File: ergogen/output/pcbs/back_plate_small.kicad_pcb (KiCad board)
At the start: 2 copper layers, 127.5 x 91.9 mm, 6 parts

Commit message: new shape
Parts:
- removed ?: , solar_system
- moved MH4 15.9 mm to (104.5, 92.8), turned to 10 degrees
- moved MH3 15.6 mm to (143.4, 98.1), turned to -15 degrees
- moved MH2 6.89 mm to (127.1, 46.3)
- moved MH5 5.62 mm to (73.6, 78.6)
- moved MH1 2.52 mm to (90.5, 47.3)
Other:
- board size 127.5 x 91.9 mm -> 130.9 x 107.2 mm

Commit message: update generated files
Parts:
- moved MH3 20.0 mm to (160.6, 108.1), turned to -30 degrees
- moved MH4 19.6 mm to (124.1, 92.9), turned to 0 degrees
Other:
- outline, holes or cut-outs redrawn
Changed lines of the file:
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@@
   (title_block
     (title "back_plate_small")
-    (date "2025-11-10")
+    (date "2025-11-12")
     (rev "1")
     (company "curtis bollinger")
@@
   (footprint "ceoloide:mounting_hole_npth"
     (layer "F.Cu")
-    (at 143.3735818 98.05513279999998 -15)
+    (at 160.64669740000002 108.05669409999999 -30)
     (property "Reference" "MH3"
-      (at 0 2.55 -15)
+      (at 0 2.55 -30)
       (layer "F.SilkS")
       hide
@@
     )
     (pad "" np_thru_hole circle
-      (at 0 0 -15)
+      (at 0 0 -30)
       (size 2.2 2.2)
       (drill 2.2)
@@
   (footprint "ceoloide:mounting_hole_npth"
     (layer "F.Cu")
-    (at 104.4990997 92.84759689999998 10)
+    (at 124.10043890000001 92.86497739999999 0)
     (property "Reference" "MH4"
-      (at 0 2.55 10)
+      (at 0 2.55 0)
       (layer "F.SilkS")
       hide
@@
     )
     (pad "" np_thru_hole circle
-      (at 0 0 10)
+      (at 0 0 0)
       (size 2.2 2.2)
       (drill 2.2)
@@
 (gr_line (start 150.55712050000002 39.4845974) (end 162.73162050000002 39.4845974) (layer Edge.Cuts) (stroke (width 0.15) (type default)))
 (gr_line (start 61.93009866331474 98.98849307597152) (end 80.90058597425492 95.64348430505513) (layer Edge.Cuts) (stroke (width 0.15) (type default)))
-(gr_line (start 49.45588610658664 51.27879995333075) (end 57.296274911602374 95.74385484982434) (layer Edge.Cuts) (stroke (width 0.15) (type default)))
+(gr_line (start 49.45588610658664 51.27879995333075) (end 57.296274911602396 95.74385484982446) (layer Edge.Cuts) (stroke (width 0.15) (type default)))
 (gr_line (start 52.70052433273374 46.64497620161837) (end 66.90353440445435 44.14060231257303) (layer Edge.Cuts) (stroke (width 0.15) (type default)))
 (gr_line (start 73.54888832016186 30.482804415970982) (end 86.68514648559608 29.564227779016903) (layer Edge.Cuts) (stroke (width 0.15) (type default)))
@@
 (gr_arc (start 66.90353444167168 44.140602323643115) (mid 69.36098474167169 42.66401712364311) (end 70.19919784167169 39.922345323643114) (layer Edge.Cuts) (stroke (width 0.15) (type default)))
 (gr_arc (start 52.70052429551636 46.6449761905481) (mid 50.118508895516364 48.2899014905481) (end 49.45588609551636 51.2787999905481) (layer Edge.Cuts) (stroke (width 0.15) (type default)))
-(gr_arc (start 57.2962749005321 95.7438548870417) (mid 58.941200200532094 98.32587028704171) (end 61.9300987005321 98.98849308704172) (layer Edge.Cuts) (stroke (width 0.15) (type default)))
+(gr_arc (start 57.296430300532116 95.74473558704183) (mid 58.94156650053212 98.32612678704183) (end 61.93009870053212 98.98849308704183) (layer Edge.Cuts) (stroke (width 0.15) (type default)))
 (gr_arc (start 85.53440973703755 98.88812249398487) (mid 83.88948443703754 96.30610709398486) (end 80.90058593703755 95.64348429398486) (layer Edge.Cuts) (stroke (width 0.15) (type default)))
 (gr_arc (start 85.95462569864738 101.2712858763529) (mid 87.59955099864739 103.85330127635291) (end 90.58844949864738 104.51592407635292) (layer Edge.Cuts) (stroke (width 0.15) (type default)))
@@
 (gr_circle (center 90.4816205 47.33459739999999) (end 91.5816205 47.33459739999999) (layer Edge.Cuts) (stroke (width 0.15) (type default)) (fill none))
 (gr_circle (center 127.12162050000002 46.33459739999999) (end 128.22162050000003 46.33459739999999) (layer Edge.Cuts) (stroke (width 0.15) (type default)) (fill none))
-(gr_circle (center 143.3735818 98.05513279999998) (end 144.4735818 98.05513279999998) (layer Edge.Cuts) (stroke (width 0.15) (type default)) (fill none))
-(gr_circle (center 104.4990997 92.84759689999998) (end 105.5990997 92.84759689999998) (layer Edge.Cuts) (stroke (width 0.15) (type default)) (fill none))
+(gr_circle (center 160.64669740000002 108.05669409999999) (end 161.74669740000002 108.05669409999999) (layer Edge.Cuts) (stroke (width 0.15) (type default)) (fill none))
+(gr_circle (center 124.10043890000001 92.86497739999999) (end 125.20043890000001 92.86497739999999) (layer Edge.Cuts) (stroke (width 0.15) (type default)) (fill none))
 (gr_circle (center 73.55589330000001 78.6000269) (end 74.6558933 78.6000269) (layer Edge.Cuts) (stroke (width 0.15) (type default)) (fill none))
 )

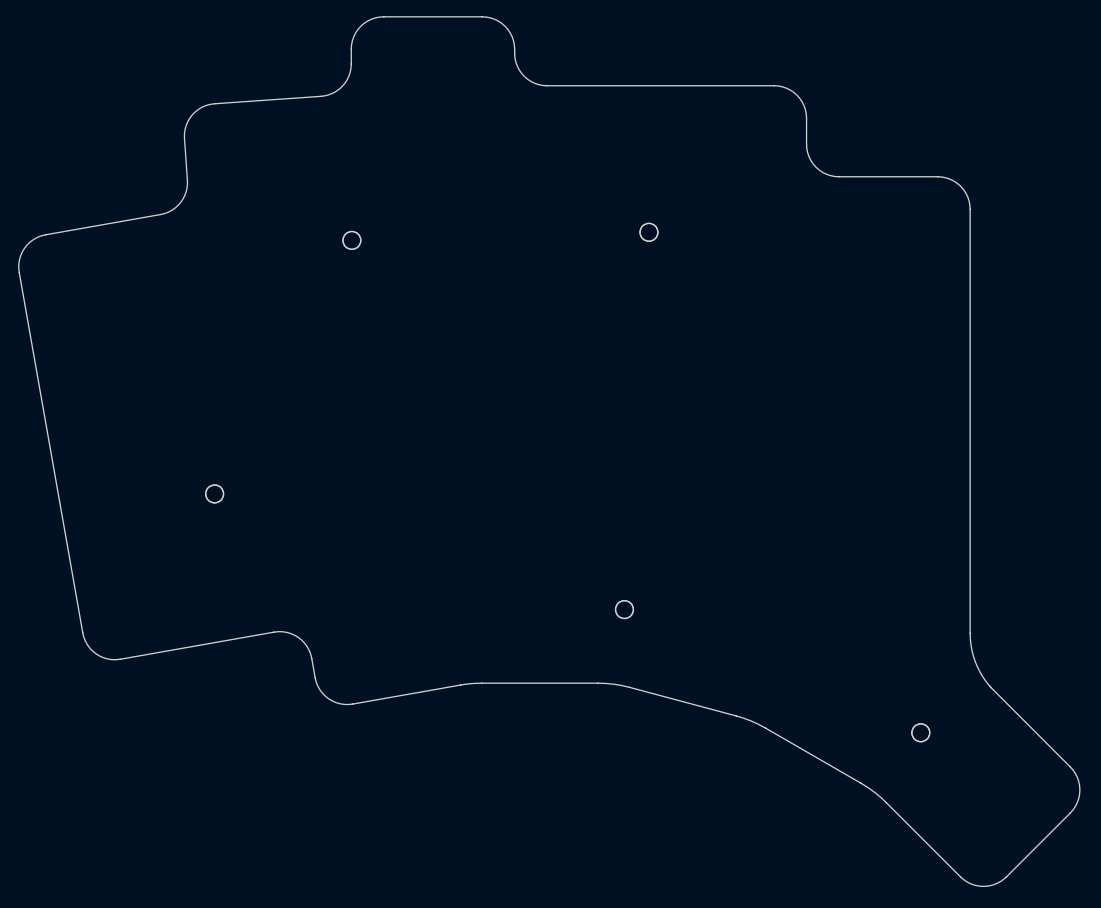
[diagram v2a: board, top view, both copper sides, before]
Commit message: working on new case
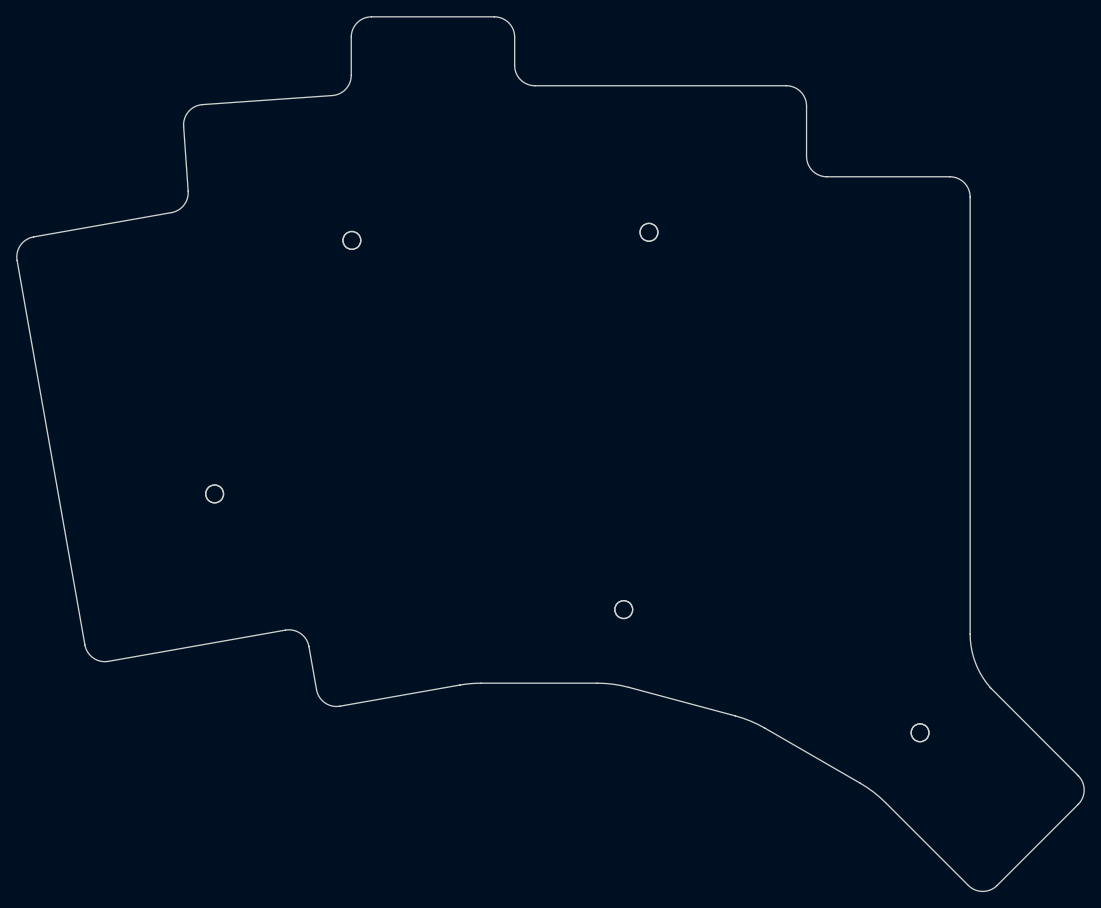
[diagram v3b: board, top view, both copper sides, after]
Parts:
- moved MH4 0.09 mm to (124.0, 92.9)
- moved MH3 0.09 mm to (160.6, 108.1)
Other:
- board size 130.9 x 107.2 mm -> 131.6 x 107.9 mm
